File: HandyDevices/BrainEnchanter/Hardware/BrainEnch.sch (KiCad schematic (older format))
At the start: 57 parts, among them Q1 MMBT2222, Q2 MMBT2222, SW1 BUTTON, SW2 BUTTON, SW3 BUTTON, SW4 BUTTON, SW5 BUTTON

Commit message: BrainEnch PCB ready for production
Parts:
- removed Q2: MMBT2222, symbol NPN_B1C2E3
- removed XTAL1: 32768, symbol CRYSTAL_H
- added L3: 10uH, IND_0805, symbol L
- added Q2: NPN, ~, symbol NPN
- added TP3: TESTPOINT, symbol TESTPOINT
- added XTAL1: 32768, CRYSTAL, symbol CRYSTAL
- R5: value 1.94k -> 81k
- R6: value 1k -> 10k
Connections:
- wire segments 159 -> 161
- no-connect marks 18 -> 17
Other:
- note removed: "WWPASS Reader G.II"
- moved on the sheet: C1, C2, C3, C4

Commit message: Current setup adjusted for R9 = 4.7k
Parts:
- R9: value 1k -> 4.7k
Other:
- note added: "R9: 1k -> 4.7k"
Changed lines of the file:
@@
 Sheet 1 1
 Title ""
-Date "11 dec 2013"
+Date "23 dec 2013"
 Rev ""
 Comp ""
@@
 P 13050 3000
 F 0 "R9" V 13130 2850 50  0000 C CNN
-F 1 "1k" V 13050 3000 50  0000 C CNN
+F 1 "4.7k" V 13050 3000 50  0000 C CNN
 F 2 "RES_0603" V 13130 3100 28  0000 C CNN
 F 3 "" H 13050 3000 60  0000 C CNN
@@
 	1    0    0    -1
 $EndComp
+Text Notes 11700 2950 0    60   ~ 0
+R9: 1k -> 4.7k
 $EndSCHEMATC

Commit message: Seems ok. Timer still not implemented.
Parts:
- removed Q2: NPN, ~, symbol NPN
- added Q2: 2N7002, symbol 2N7002
- R7: value 6.5k -> 6.8k
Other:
- note added: "BC848 replaced\nwith 2N7002 to\neliminate B-E\ncurrent"
- note added: "C16: Do not mount"
- note added: "R7: 6.5k -> 6.8k"
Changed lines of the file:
@@
 Sheet 1 1
 Title ""
-Date "23 dec 2013"
+Date "2 jan 2014"
 Rev ""
 Comp ""
@@
 P 12350 4850
 F 0 "R7" V 12430 4700 50  0000 C CNN
-F 1 "6.5k" V 12350 4850 50  0000 C CNN
+F 1 "6.8k" V 12350 4850 50  0000 C CNN
 F 2 "RES_0603" V 12430 4950 28  0000 C CNN
 F 3 "~" H 12350 4850 60  0000 C CNN
@@
 Wire Wire Line
 	14200 3100 14800 3100
-Wire Wire Line
-	14800 3000 14800 3200
 Connection ~ 14800 3100
 Wire Wire Line
 	14800 3700 14800 4200
 Wire Wire Line
-	14800 2250 14800 2600
+	14800 2250 14800 2650
 Wire Wire Line
 	13050 1950 13050 2150
@@
 Wire Wire Line
 	2950 3650 3000 3650
-$Comp
-L NPN Q2
-U 1 1 52A82105
-P 14750 2800
-F 0 "Q2" H 14950 2850 60  0000 C CNN
-F 1 "NPN" H 15000 2750 60  0000 C CNN
-F 2 "~" H 14750 2800 60  0000 C CNN
-F 3 "~" H 14750 2800 60  0000 C CNN
-	1    14750 2800
-	1    0    0    -1
-$EndComp
 Text Notes 11700 2950 0    60   ~ 0
 R9: 1k -> 4.7k
+$Comp
+L 2N7002 Q2
+U 1 1 52C57941
+P 14750 2850
+F 0 "Q2" H 14950 2900 60  0000 C CNN
+F 1 "2N7002" H 15100 2800 60  0000 C CNN
+F 2 "" H 14750 2850 60  0000 C CNN
+F 3 "" H 14750 2850 60  0000 C CNN
+	1    14750 2850
+	1    0    0    -1
+$EndComp
+Wire Wire Line
+	14800 3200 14800 3050
+Text Notes 15250 2550 0    60   ~ 0
+BC848 replaced\nwith 2N7002 to\neliminate B-E\ncurrent
+Text Notes 12100 5050 0    60   ~ 0
+R7: 6.5k -> 6.8k
+Text Notes 12800 9700 0    60   ~ 0
+C16: Do not mount
 $EndSCHEMATC

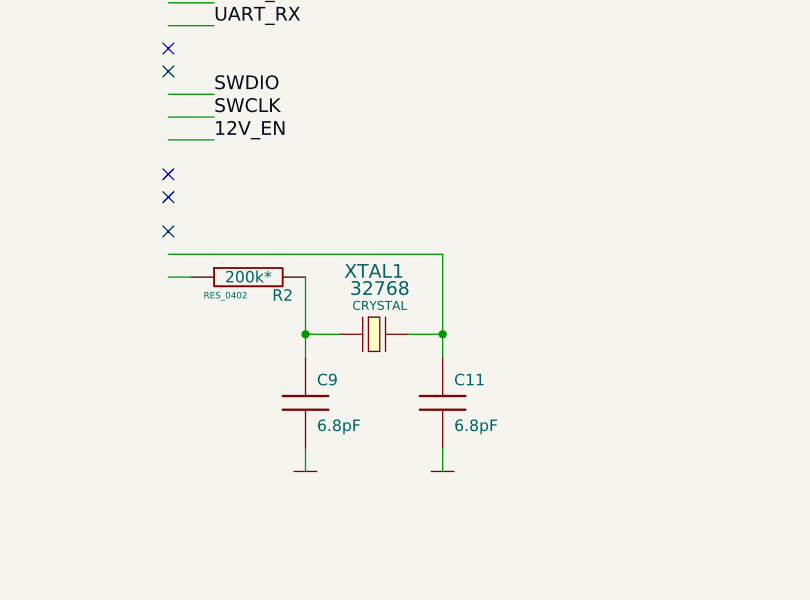
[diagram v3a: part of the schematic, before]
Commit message: Crystal sch changed
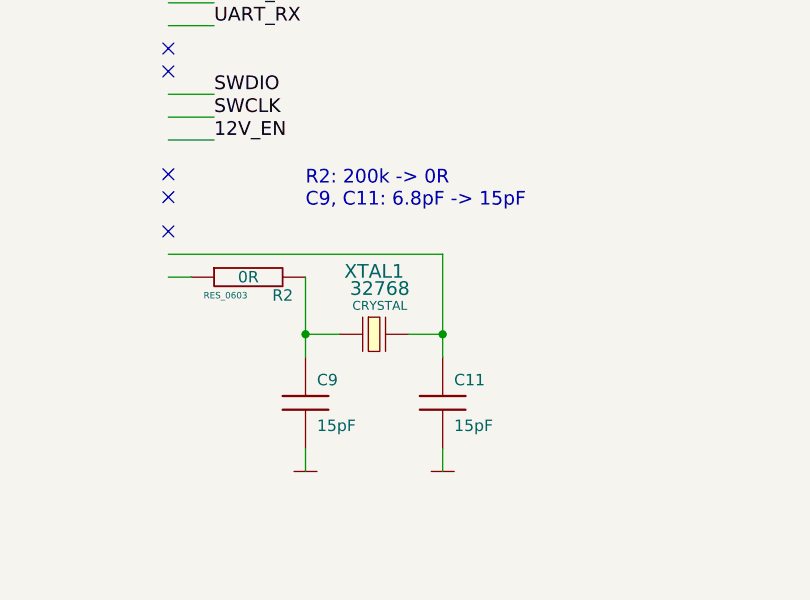
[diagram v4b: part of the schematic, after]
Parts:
- C11, C9: value 6.8pF -> 15pF
- R2: value 200k* -> 0R; footprint RES_0402 -> RES_0603
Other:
- note added: "R2: 200k -> 0R\nC9, C11: 6.8pF -> 15pF"
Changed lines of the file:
@@
 Sheet 1 1
 Title ""
-Date "2 jan 2014"
+Date "4 jan 2014"
 Rev ""
 Comp ""
@@
 P 7050 3950
 F 0 "C9" H 7100 4050 50  0000 L CNN
-F 1 "6.8pF" H 7100 3850 50  0000 L CNN
+F 1 "15pF" H 7100 3850 50  0000 L CNN
 F 2 "" H 7050 3950 60  0001 C CNN
 F 3 "" H 7050 3950 60  0001 C CNN
@@
 P 7650 3950
 F 0 "C11" H 7700 4050 50  0000 L CNN
-F 1 "6.8pF" H 7700 3850 50  0000 L CNN
+F 1 "15pF" H 7700 3850 50  0000 L CNN
 F 2 "" H 7650 3950 60  0001 C CNN
 F 3 "" H 7650 3950 60  0001 C CNN
@@
 P 6800 3400
 F 0 "R2" V 6880 3250 50  0000 C CNN
-F 1 "200k*" V 6800 3400 50  0000 C CNN
-F 2 "RES_0402" V 6880 3500 28  0000 C CNN
+F 1 "0R" V 6800 3400 50  0000 C CNN
+F 2 "RES_0603" V 6880 3500 28  0000 C CNN
 F 3 "~" H 6800 3400 60  0000 C CNN
 	1    6800 3400
@@
 Text Notes 12800 9700 0    60   ~ 0
 C16: Do not mount
+Text Notes 7050 3100 0    60   ~ 0
+R2: 200k -> 0R\nC9, C11: 6.8pF -> 15pF
 $EndSCHEMATC
